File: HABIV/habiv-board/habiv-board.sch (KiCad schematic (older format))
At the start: 108 parts, among them IC1 RTC_PCF8523T, J1 Micro_SD_Card_Det, J2 Conn_ARM_JTAG_SWD_20, J3 Conn_01x02_Male, J4 Conn_01x16_Male, J5 Conn_01x02_Male, J6 Conn_01x16_Male, J7 Conn_01x16_Male, J9 Conn_01x02_Male, Q1 32.768KHz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

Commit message: finish submodules and combine
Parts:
- added R100: 0k1, Resistor_SMD:R_0805_2012Metric, symbol Device:R_Small
- added R101: 0k2, Resistor_SMD:R_0805_2012Metric, symbol Device:R_Small
- renumbered B1 to B2
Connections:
- wire segments 371 -> 373
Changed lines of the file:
@@
 $EndComp
 $Comp
-L habiv-board-rescue:BATTERY-real_time_clock-eagle-import B1
+L habiv-board-rescue:BATTERY-real_time_clock-eagle-import B2
 U 1 1 5BBEE532
 P 3950 3450
-F 0 "B1" V 3996 3317 50  0000 R CNN
+F 0 "B2" V 3996 3317 50  0000 R CNN
 F 1 "CR1220" V 3905 3317 50  0000 R CNN
 F 2 "S8411-45R:S8411-45R" H 3950 3450 50  0001 L BNN
@@
 P 1750 3150
 F 0 "R3" H 1800 3200 50  0000 L CNN
-F 1 "8.2k" H 1900 3200 50  0000 L CNN
+F 1 "8.2k" H 1800 3050 50  0000 L CNN
 F 2 "Resistor_SMD:R_0805_2012Metric" H 1750 3150 50  0001 C CNN
 F 3 "~" H 1750 3150 50  0001 C CNN
@@
 U 1 1 5CCE56CA
 P 2250 14800
-F 0 "R9" H 2309 14846 50  0000 L CNN
-F 1 "56k" H 2309 14755 50  0000 L CNN
+F 0 "R9" H 2250 14950 50  0000 L CNN
+F 1 "56k" V 2250 14750 50  0000 L CNN
 F 2 "Resistor_SMD:R_0805_2012Metric" H 2250 14800 50  0001 C CNN
 F 3 "~" H 2250 14800 50  0001 C CNN
@@
 U 1 1 5D398530
 P 2250 14600
-F 0 "R8" H 2320 14646 50  0000 L CNN
+F 0 "R8" H 2200 14650 50  0000 L CNN
 F 1 "0" V 2250 14550 50  0000 L CNN
 F 2 "Resistor_SMD:R_0805_2012Metric" V 2180 14600 50  0001 C CNN
@@
 U 1 1 5D574AA1
 P 2450 14100
-F 0 "R13" H 2520 14146 50  0000 L CNN
+F 0 "R13" H 2400 13950 50  0000 L CNN
 F 1 "0" V 2450 14050 50  0000 L CNN
 F 2 "Resistor_SMD:R_0805_2012Metric" V 2380 14100 50  0001 C CNN
@@
 $EndComp
 Wire Wire Line
-	2850 7900 3450 7900
-Wire Wire Line
-	2850 8200 3450 8200
+	2850 7900 3150 7900
+Wire Wire Line
+	2850 8200 3150 8200
 Wire Wire Line
 	4900 6500 4900 7350
+$Comp
+L Device:R_Small R100
+U 1 1 5CB107A7
+P 3250 7900
+F 0 "R100" V 3150 7900 50  0000 C CNN
+F 1 "0k1" V 3350 7900 50  0000 C CNN
+F 2 "Resistor_SMD:R_0805_2012Metric" H 3250 7900 50  0001 C CNN
+F 3 "~" H 3250 7900 50  0001 C CNN
+	1    3250 7900
+	0    1    1    0
+$EndComp
+Wire Wire Line
+	3350 7900 3450 7900
+$Comp
+L Device:R_Small R101
+U 1 1 5CB10998
+P 3250 8200
+F 0 "R101" V 3150 8200 50  0000 C CNN
+F 1 "0k2" V 3350 8200 50  0000 C CNN
+F 2 "Resistor_SMD:R_0805_2012Metric" H 3250 8200 50  0001 C CNN
+F 3 "~" H 3250 8200 50  0001 C CNN
+	1    3250 8200
+	0    1    1    0
+$EndComp
+Wire Wire Line
+	3350 8200 3450 8200
 $EndSCHEMATC

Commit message: fix power system layout on habiv
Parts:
- added J10, J8: Conn_01x08_Male, Connector_PinHeader_2.54mm:PinHeader_1x08_P2.54mm_Vertical, symbol Connector:Conn_01x08_Male
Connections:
- wire segments 373 -> 412
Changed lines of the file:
@@
 $EndComp
 Wire Wire Line
-	18500 6900 18850 6900
+	18500 6900 18750 6900
 $Comp
 L power:GND #PWR0102
@@
 $EndComp
 Wire Wire Line
-	18500 7750 18850 7750
+	18500 7750 18750 7750
 $Comp
 L power:+3V3 #PWR0103
@@
 $EndComp
 Wire Wire Line
-	18500 5800 18850 5800
+	18500 5800 18750 5800
 Wire Wire Line
-	18500 6650 19150 6650
+	18500 6650 19000 6650
 $Comp
 L power:GND #PWR0104
@@
 Wire Wire Line
 	3350 8200 3450 8200
+$Comp
+L Connector:Conn_01x08_Male J8
+U 1 1 5CAC32FD
+P 19450 6200
+F 0 "J8" H 19423 6080 50  0000 R CNN
+F 1 "Conn_01x08_Male" H 19423 6171 50  0000 R CNN
+F 2 "Connector_PinHeader_2.54mm:PinHeader_1x08_P2.54mm_Vertical" H 19450 6200 50  0001 C CNN
+F 3 "~" H 19450 6200 50  0001 C CNN
+	1    19450 6200
+	-1   0    0    1
+$EndComp
+$Comp
+L Connector:Conn_01x08_Male J10
+U 1 1 5CB7DDCF
+P 19450 7400
+F 0 "J10" H 19423 7280 50  0000 R CNN
+F 1 "Conn_01x08_Male" H 19423 7371 50  0000 R CNN
+F 2 "Connector_PinHeader_2.54mm:PinHeader_1x08_P2.54mm_Vertical" H 19450 7400 50  0001 C CNN
+F 3 "~" H 19450 7400 50  0001 C CNN
+	1    19450 7400
+	-1   0    0    1
+$EndComp
+Wire Wire Line
+	18750 5800 18750 5900
+Wire Wire Line
+	18750 5900 19050 5900
+Connection ~ 18750 5800
+Wire Wire Line
+	18750 5800 18850 5800
+Wire Wire Line
+	19050 5900 19050 5800
+Wire Wire Line
+	19050 5800 19250 5800
+Connection ~ 19050 5900
+Wire Wire Line
+	19050 5900 19250 5900
+Wire Wire Line
+	19050 5900 19050 6000
+Wire Wire Line
+	19050 6000 19250 6000
+Wire Wire Line
+	19050 6000 19050 6100
+Wire Wire Line
+	19050 6100 19250 6100
+Connection ~ 19050 6000
+Wire Wire Line
+	19000 6650 19000 6500
+Wire Wire Line
+	19000 6200 19250 6200
+Connection ~ 19000 6650
+Wire Wire Line
+	19000 6650 19150 6650
+Wire Wire Line
+	19000 6300 19250 6300
+Connection ~ 19000 6300
+Wire Wire Line
+	19000 6300 19000 6200
+Wire Wire Line
+	19000 6400 19250 6400
+Connection ~ 19000 6400
+Wire Wire Line
+	19000 6400 19000 6300
+Wire Wire Line
+	19000 6500 19250 6500
+Connection ~ 19000 6500
+Wire Wire Line
+	19000 6500 19000 6400
+Wire Wire Line
+	18750 6900 18750 7000
+Wire Wire Line
+	18750 7000 19050 7000
+Connection ~ 18750 6900
+Wire Wire Line
+	18750 6900 18850 6900
+Wire Wire Line
+	19050 7000 19050 7100
+Wire Wire Line
+	19050 7300 19250 7300
+Connection ~ 19050 7000
+Wire Wire Line
+	19050 7000 19250 7000
+Wire Wire Line
+	19050 7100 19250 7100
+Connection ~ 19050 7100
+Wire Wire Line
+	19050 7100 19050 7200
+Wire Wire Line
+	19050 7200 19250 7200
+Connection ~ 19050 7200
+Wire Wire Line
+	19050 7200 19050 7300
+Wire Wire Line
+	18750 7750 18750 7400
+Wire Wire Line
+	18750 7400 19050 7400
+Connection ~ 18750 7750
+Wire Wire Line
+	18750 7750 18850 7750
+Wire Wire Line
+	19050 7400 19050 7500
+Wire Wire Line
+	19050 7700 19250 7700
+Connection ~ 19050 7400
+Wire Wire Line
+	19050 7400 19250 7400
+Wire Wire Line
+	19050 7600 19250 7600
+Connection ~ 19050 7600
+Wire Wire Line
+	19050 7600 19050 7700
+Wire Wire Line
+	19050 7500 19250 7500
+Connection ~ 19050 7500
+Wire Wire Line
+	19050 7500 19050 7600
 $EndSCHEMATC

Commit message: fix some schematic errorS
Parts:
- removed D1: 1N4148, Adafruit Ultimate GPS:SOD-323, symbol habiv-board-rescue:DIODESOD-323-Adafruit_Ultimate_GPS-eagle-import
- removed R10, R5, R6, R7, R9: 56k, Resistor_SMD:R_0805_2012Metric, symbol Device:R_Small
- removed R29, R30: 1K, Resistor_SMD:R_0805_2012Metric, symbol habiv-board-rescue:RESISTOR0805_NOOUTLINE-real_time_clock-eagle-import
- removed R4: 0, Resistor_SMD:R_0805_2012Metric, symbol Device:R
- C1, C4: symbol habiv-board-rescue:CAP_CERAMIC0805-NOOUTLINE-real_time_clock-eagle-import -> Device:C_Small
- C7: symbol habiv-board-rescue:CAP_CERAMIC0805-NOOUTLINE-Adafruit_Ultimate_GPS-eagle-import -> Device:C_Small
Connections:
- net labels added: ALTI_CS, DET_A, DET_B, DRDY_M, GPS_RX, GPS_TX, INT1_AG, INT2_AG, INT_M, SCK, SCL, SCLK, SDA, SDI-SDA, SDO, SDO_AG, SDO_M, SD_CD, THERMO_CS
- net labels removed: +3.3VA, 1PPS, PS, VBACKUP, VDD
- wire segments 412 -> 434
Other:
- note added: "C18: 1nF Minimum must be guaranteed under an 11V bias condition\n"
- note added: "NOTE: PA10 IN CODE"
- note added: "NOTE: PA9 IN CODE \n"
- moved on the sheet: C11, C19

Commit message: some work on layout redo
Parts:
- removed J10, J8: Conn_01x08_Male, Connector_PinHeader_2.54mm:PinHeader_1x08_P2.54mm_Vertical, symbol Connector:Conn_01x08_Male
- added J10, J8: Conn_02x04_Counter_Clockwise, Connector_PinHeader_2.54mm:PinHeader_2x04_P2.54mm_Vertical, symbol Connector_Generic:Conn_02x04_Counter_Clockwise
- added TP1, TP10, TP2, TP3, TP4, TP5, TP6, TP7, TP8, TP9: TestPoint, TestPoint:TestPoint_Pad_D1.0mm, symbol Connector:TestPoint
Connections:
- wire segments 434 -> 458

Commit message: :art: Fix layout connections for new schematic
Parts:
- removed R24: 10K, Resistor_SMD:R_0805_2012Metric, symbol habiv-board-rescue:RESISTOR0805_NOOUTLINE-Adafruit_Ultimate_GPS-eagle-import
- added TP11, TP12: TestPoint, symbol Connector:TestPoint
- C1, C4: value 10uF -> 10u
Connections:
- net +3V3: now also C1.1, R16.1
- net GND: now also C1.2, C4.2
- net PB4: now also TP11.1
- net RST: now also TP12.1
- net at R1.1, R16.2: now also C4.1
- net 3.3V: no longer names the net of R25.2, U3.P$1 (VCC)
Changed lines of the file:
@@
 	2850 2200 2850 2100
 $Comp
-L Device:C_Small C4
-U 1 0 E7D47EA7
-P 2850 2400
-F 0 "C4" H 3000 2500 50  0000 C CNN
-F 1 "10uF" H 3050 2400 50  0000 C CNN
-F 2 "Capacitor_SMD:C_0805_2012Metric" H 2850 2400 50  0001 C CNN
-F 3 "" H 2850 2400 50  0001 C CNN
-	1    2850 2400
-	1    0    0    -1
-$EndComp
-$Comp
 L habiv-board-rescue:RTC_PCF8523T-real_time_clock-eagle-import IC1
 U 1 0 22F7723E
@@
 	0    1    1    0
 $EndComp
-$Comp
-L habiv-board-rescue:VCC-real_time_clock-eagle-import #P+02
-U 1 0 637B3A6A
-P 2850 1500
-F 0 "#P+02" H 2850 1500 50  0001 C CNN
-F 1 "VCC" V 2950 1600 59  0000 R TNN
-F 2 "" H 2850 1500 50  0001 C CNN
-F 3 "" H 2850 1500 50  0001 C CNN
-	1    2850 1500
-	-1   0    0    -1
-$EndComp
-$Comp
-L Device:C_Small C1
-U 1 0 8350CC17
-P 2350 1800
-F 0 "C1" H 2200 1900 50  0000 C CNN
-F 1 "10uF" H 2150 1800 50  0000 C CNN
-F 2 "Capacitor_SMD:C_0805_2012Metric" H 2350 1800 50  0001 C CNN
-F 3 "" H 2350 1800 50  0001 C CNN
-	1    2350 1800
-	1    0    0    -1
-$EndComp
-$Comp
-L habiv-board-rescue:VCC-real_time_clock-eagle-import #P+01
-U 1 0 48C2C5DB
-P 2350 1500
-F 0 "#P+01" H 2350 1500 50  0001 C CNN
-F 1 "VCC" V 2450 1600 59  0000 R TNN
-F 2 "" H 2350 1500 50  0001 C CNN
-F 3 "" H 2350 1500 50  0001 C CNN
-	1    2350 1500
-	-1   0    0    -1
-$EndComp
 Connection ~ 2850 2200
 $Comp
@@
 Wire Wire Line
 	13050 14450 12450 14450
-Text Label 11450 14250 0    10   ~ 0
-3.3V
 Wire Wire Line
 	13050 15250 12900 15250
@@
 	13050 15350 12900 15350
 Wire Wire Line
-	11950 16250 11950 16150
-Connection ~ 12350 15350
-Wire Wire Line
 	14250 15350 14450 15350
 $Comp
@@
 $EndComp
 $Comp
-L habiv-board-rescue:RESISTOR0805_NOOUTLINE-Adafruit_Ultimate_GPS-eagle-import R24
-U 1 0 4F14531CD85E66C8
-P 11950 15950
-F 0 "R24" H 11950 16050 50  0000 C CNN
-F 1 "10K" H 11950 15950 40  0000 C CNB
-F 2 "Resistor_SMD:R_0805_2012Metric" H 11950 15950 50  0001 C CNN
-F 3 "" H 11950 15950 50  0001 C CNN
-	1    11950 15950
-	0    1    1    0
-$EndComp
-$Comp
 L habiv-board-rescue:U.FL-Adafruit_Ultimate_GPS-eagle-import U$1
 U 1 0 14A4E007DC93C178
@@
 	1    0    0    -1
 $EndComp
-Text GLabel 6350 14350 2    60   Input ~ 0
+Text GLabel 6700 14350 2    60   Input ~ 0
 PB4
 Text GLabel 6650 15050 2    60   Input ~ 0
@@
 Text GLabel 6650 14950 2    60   Input ~ 0
 PB3
-Text GLabel 6350 14450 2    60   Input ~ 0
+Text GLabel 6700 14450 2    60   Input ~ 0
 RST
 $Comp
@@
 PB6
 Wire Wire Line
-	12350 16250 11950 16250
-Wire Wire Line
-	12350 15350 12350 16250
-Wire Wire Line
 	10400 2800 10550 2800
 Wire Wire Line
@@
 Wire Wire Line
 	5650 13850 5650 13950
-$Comp
-L Device:R R25
-U 1 1 5D048A73
-P 12450 13900
-F 0 "R25" H 12520 13946 50  0000 L CNN
-F 1 "0" V 12450 13850 50  0000 L CNN
-F 2 "Resistor_SMD:R_0805_2012Metric" V 12380 13900 50  0001 C CNN
-F 3 "~" H 12450 13900 50  0001 C CNN
-	1    12450 13900
-	1    0    0    -1
-$EndComp
-Wire Wire Line
-	12450 14050 12450 14150
 Wire Wire Line
 	12450 14150 12450 14450
@@
 	0    1    1    0
 $EndComp
-Wire Wire Line
-	12600 15350 12350 15350
 $Comp
 L Device:R R8
@@
 	1    0    0    -1
 $EndComp
-Wire Wire Line
-	11450 14150 11450 14350
 Text Label 1900 3200 0    50   ~ 0
 SCL
@@
 Wire Wire Line
 	16400 9850 16500 9850
-Wire Wire Line
-	11750 15350 12350 15350
 $Comp
 L power:GND #PWR0109
@@
 THERMO_CS
 Wire Wire Line
-	2350 1700 2350 1600
+	1800 1250 1800 1150
 Wire Wire Line
 	2850 2300 2850 2200
@@
 $EndComp
 $Comp
-L power:+3V3 #PWR0106
-U 1 1 5CC71CF3
-P 11950 15750
-F 0 "#PWR0106" H 11950 15600 50  0001 C CNN
-F 1 "+3V3" H 11965 15923 50  0000 C CNN
-F 2 "" H 11950 15750 50  0001 C CNN
-F 3 "" H 11950 15750 50  0001 C CNN
-	1    11950 15750
-	1    0    0    -1
-$EndComp
-$Comp
 L power:+3V3 #PWR0110
 U 1 1 5CCA1BA9
@@
 $EndComp
 Connection ~ 3800 8950
-Wire Wire Line
-	2850 1700 2850 1600
 $Comp
 L power:GND #PWR0111
 U 1 1 5CD8DED2
-P 2350 1900
-F 0 "#PWR0111" H 2350 1650 50  0001 C CNN
-F 1 "GND" H 2355 1727 50  0000 C CNN
-F 2 "" H 2350 1900 50  0001 C CNN
-F 3 "" H 2350 1900 50  0001 C CNN
-	1    2350 1900
+P 1800 1450
+F 0 "#PWR0111" H 1800 1200 50  0001 C CNN
+F 1 "GND" H 1805 1277 50  0000 C CNN
+F 2 "" H 1800 1450 50  0001 C CNN
+F 3 "" H 1800 1450 50  0001 C CNN
+	1    1800 1450
 	1    0    0    -1
 $EndComp
@@
 Wire Wire Line
 	7450 6550 7550 6550
+Wire Wire Line
+	12450 14050 12450 14150
+$Comp
+L Device:R R25
+U 1 1 5D048A73
+P 12450 13900
+F 0 "R25" H 12520 13946 50  0000 L CNN
+F 1 "0" V 12450 13850 50  0000 L CNN
+F 2 "Resistor_SMD:R_0805_2012Metric" V 12380 13900 50  0001 C CNN
+F 3 "~" H 12450 13900 50  0001 C CNN
+	1    12450 13900
+	1    0    0    -1
+$EndComp
+Wire Wire Line
+	11750 15350 12600 15350
+Wire Wire Line
+	2850 1600 2850 1700
+$Comp
+L power:+3V3 #PWR0106
+U 1 1 5CE9524D
+P 1800 1150
+F 0 "#PWR0106" H 1800 1000 50  0001 C CNN
+F 1 "+3V3" H 1815 1323 50  0000 C CNN
+F 2 "" H 1800 1150 50  0001 C CNN
+F 3 "" H 1800 1150 50  0001 C CNN
+	1    1800 1150
+	1    0    0    -1
+$EndComp
+$Comp
+L power:+3V3 #PWR0114
+U 1 1 5CECA70E
+P 2850 1600
+F 0 "#PWR0114" H 2850 1450 50  0001 C CNN
+F 1 "+3V3" H 2865 1773 50  0000 C CNN
+F 2 "" H 2850 1600 50  0001 C CNN
+F 3 "" H 2850 1600 50  0001 C CNN
+	1    2850 1600
+	1    0    0    -1
+$EndComp
+Wire Wire Line
+	11450 14150 11450 14350
+$Comp
+L Device:C_Small C1
+U 1 1 5CF77CD4
+P 1800 1350
+F 0 "C1" H 1892 1396 50  0000 L CNN
+F 1 "10u" H 1892 1305 50  0000 L CNN
+F 2 "Capacitor_SMD:C_0805_2012Metric" H 1800 1350 50  0001 C CNN
+F 3 "~" H 1800 1350 50  0001 C CNN
+	1    1800 1350
+	1    0    0    -1
+$EndComp
+$Comp
+L Device:C_Small C4
+U 1 1 5CF784EA
+P 2850 2400
+F 0 "C4" H 2942 2446 50  0000 L CNN
+F 1 "10u" H 2942 2355 50  0000 L CNN
+F 2 "Capacitor_SMD:C_0805_2012Metric" H 2850 2400 50  0001 C CNN
+F 3 "~" H 2850 2400 50  0001 C CNN
+	1    2850 2400
+	1    0    0    -1
+$EndComp
+$Comp
+L Connector:TestPoint TP11
+U 1 1 5D017C96
+P 6450 14100
+F 0 "TP11" H 6508 14220 50  0000 L CNN
+F 1 "TestPoint" H 6508 14129 50  0000 L CNN
+F 2 "" H 6650 14100 50  0001 C CNN
+F 3 "~" H 6650 14100 50  0001 C CNN
+	1    6450 14100
+	1    0    0    -1
+$EndComp
+$Comp
+L Connector:TestPoint TP12
+U 1 1 5D017E50
+P 7000 14100
+F 0 "TP12" H 7058 14220 50  0000 L CNN
+F 1 "TestPoint" H 7058 14129 50  0000 L CNN
+F 2 "" H 7200 14100 50  0001 C CNN
+F 3 "~" H 7200 14100 50  0001 C CNN
+	1    7000 14100
+	1    0    0    -1
+$EndComp
+Wire Wire Line
+	6350 14350 6450 14350
+Wire Wire Line
+	6450 14350 6450 14100
+Connection ~ 6450 14350
+Wire Wire Line
+	6450 14350 6700 14350
+Wire Wire Line
+	6350 14450 6600 14450
+Wire Wire Line
+	6600 14450 6600 14200
+Wire Wire Line
+	6600 14200 7000 14200
+Connection ~ 6600 14450
+Wire Wire Line
+	6600 14450 6700 14450
+Wire Wire Line
+	7000 14200 7000 14100
 $EndSCHEMATC

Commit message: fix all drc errors
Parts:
- C7: value 0.1uF -> 0.1u
- TP11, TP12: footprint (none) -> TestPoint:TestPoint_Pad_D1.0mm
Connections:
- net SCLK is gone; now on net PA5: R21.2, R31.2, R8.2
- net GND: now also C7.2
- net at R25.2, U3.P$1 (VCC): now also C7.1
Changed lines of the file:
@@
-$EndComp
-$Comp
-L Device:C_Small C7
-U 1 0 24498BA92B08E60C
-P 11450 14450
-F 0 "C7" V 11360 14499 50  0000 C CNN
-F 1 "0.1uF" V 11540 14499 50  0000 C CNN
-F 2 "Capacitor_SMD:C_0805_2012Metric" H 11450 14450 50  0001 C CNN
-F 3 "" H 11450 14450 50  0001 C CNN
-	1    11450 14450
-	1    0    0    -1
 $EndComp
 $Comp
@@
 PA5
 Text Label 6600 6250 0    50   ~ 0
-SCK
+SCLK
 Wire Wire Line
 	6250 6250 6400 6250
@@
 F 0 "TP11" H 6508 14220 50  0000 L CNN
 F 1 "TestPoint" H 6508 14129 50  0000 L CNN
-F 2 "" H 6650 14100 50  0001 C CNN
+F 2 "TestPoint:TestPoint_Pad_D1.0mm" H 6650 14100 50  0001 C CNN
 F 3 "~" H 6650 14100 50  0001 C CNN
 	1    6450 14100
@@
 F 0 "TP12" H 7058 14220 50  0000 L CNN
 F 1 "TestPoint" H 7058 14129 50  0000 L CNN
-F 2 "" H 7200 14100 50  0001 C CNN
+F 2 "TestPoint:TestPoint_Pad_D1.0mm" H 7200 14100 50  0001 C CNN
 F 3 "~" H 7200 14100 50  0001 C CNN
 	1    7000 14100
@@
 Wire Wire Line
 	7000 14200 7000 14100
+$Comp
+L Device:C_Small C7
+U 1 1 5CCBB00E
+P 11450 14450
+F 0 "C7" H 11542 14496 50  0000 L CNN
+F 1 "0.1u" H 11542 14405 50  0000 L CNN
+F 2 "Capacitor_SMD:C_0805_2012Metric" H 11450 14450 50  0001 C CNN
+F 3 "~" H 11450 14450 50  0001 C CNN
+	1    11450 14450
+	1    0    0    -1
+$EndComp
 $EndSCHEMATC

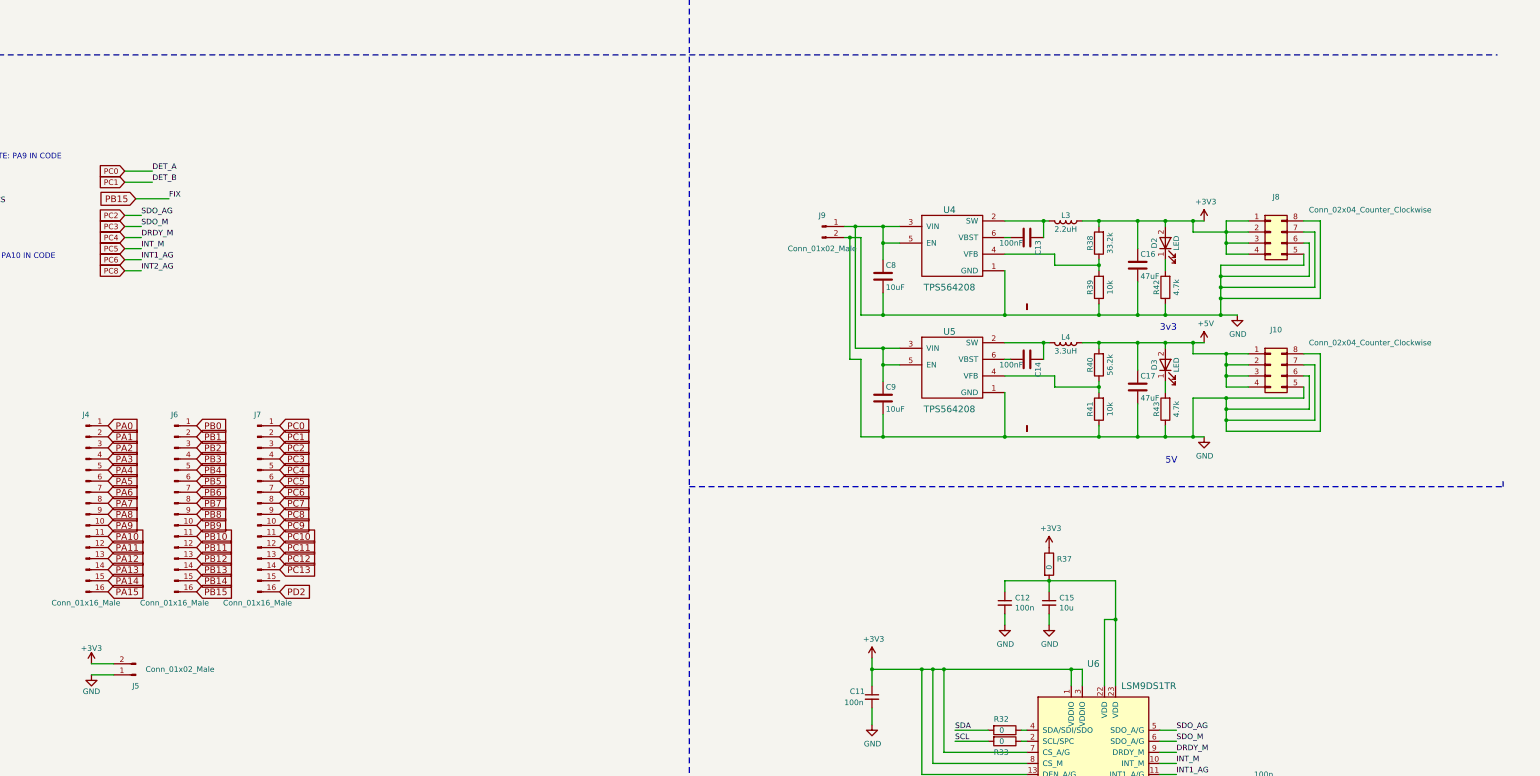
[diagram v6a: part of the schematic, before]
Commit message: add xt30 connectors
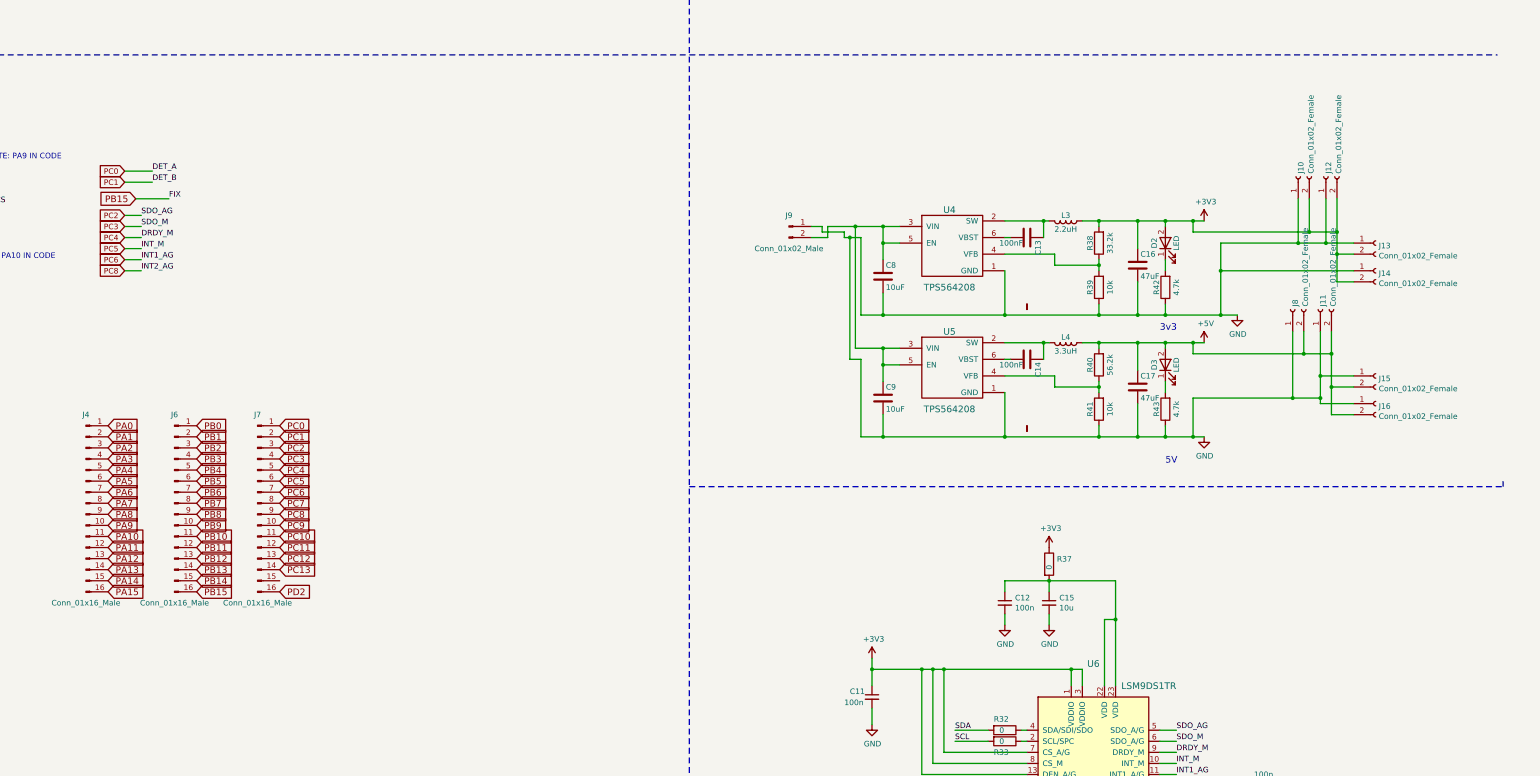
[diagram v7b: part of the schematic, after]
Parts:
- removed J10, J8: Conn_02x04_Counter_Clockwise, Connector_PinHeader_2.54mm:PinHeader_2x04_P2.54mm_Vertical, symbol Connector_Generic:Conn_02x04_Counter_Clockwise
- removed J5: Conn_01x02_Male, Connector_PinHeader_2.54mm:PinHeader_1x02_P2.54mm_Vertical, symbol habiv-board-rescue:Conn_01x02_Male-STM32-rescue
- added J10, J11, J12, J13, J14, J15, J16, J8: Conn_01x02_Female, Connector_AMASS:AMASS_XT30U-F_1x02_P5.0mm_Vertical, symbol Connector:Conn_01x02_Female
- J9: footprint Connector_PinHeader_2.54mm:PinHeader_1x02_P2.54mm_Vertical -> Connector_AMASS:AMASS_XT30U-M_1x02_P5.0mm_Vertical
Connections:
- net +3V3: now also J10.2 (Pin_2), J12.2 (Pin_2), J13.2 (Pin_2), J14.2 (Pin_2)
- net +5V: now also J11.2 (Pin_2), J15.2 (Pin_2), J16.2 (Pin_2), J8.2 (Pin_2)
- net GND: now also J9.1 (Pin_1), J10.1 (Pin_1), J11.1 (Pin_1), J12.1 (Pin_1), J13.1 (Pin_1), J14.1 (Pin_1), J15.1 (Pin_1), J16.1 (Pin_1), J8.1 (Pin_1); no longer J9.2 (Pin_2)
- net at C8.1, C9.1, U4.3 (VIN)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: now also J9.2 (Pin_2); no longer J9.1 (Pin_1)
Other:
- moved on the sheet: J9
